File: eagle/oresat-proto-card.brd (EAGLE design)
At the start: 99.8 x 94.7 mm, 126 parts, among them J1 J-SAMTEC-TFM-110-X1-XXX-D-RA, J2 U.FL, J3 U.FL, J4 U.FL, J6 J-SAMTEC-TFM-120-X1-XXX-D-RA, J7 ORESAT-DEBUG-CONNECTOR-SOLAR, Q1 DMP2240UDM, Q3 MOSFET-PCH-SOT23-6, Q4 MOSFET-PCH-SOT23-6, Q5 PMV45EN, Q6 PMV45EN, U1 TCAN330, U3 MAX7310ATE, U4 MAX4211FETE, U5 TPS62111RSA, U7 STM32F091C, U8 MIC842LYC5, U9 MIC842LYC5, X2 16MHZ-2.5x2mm

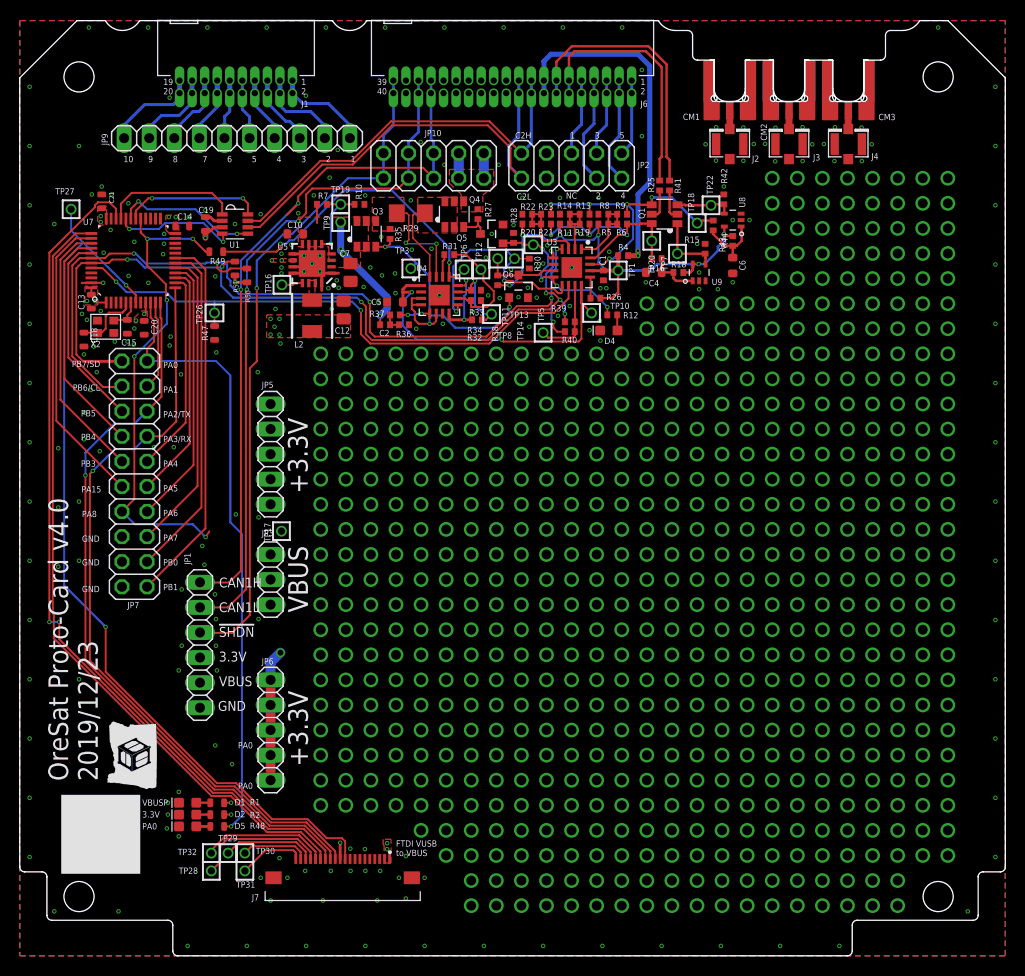
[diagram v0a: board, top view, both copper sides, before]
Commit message: swapped 0402 to 0603 where necessary, fixed labels on tnames layer
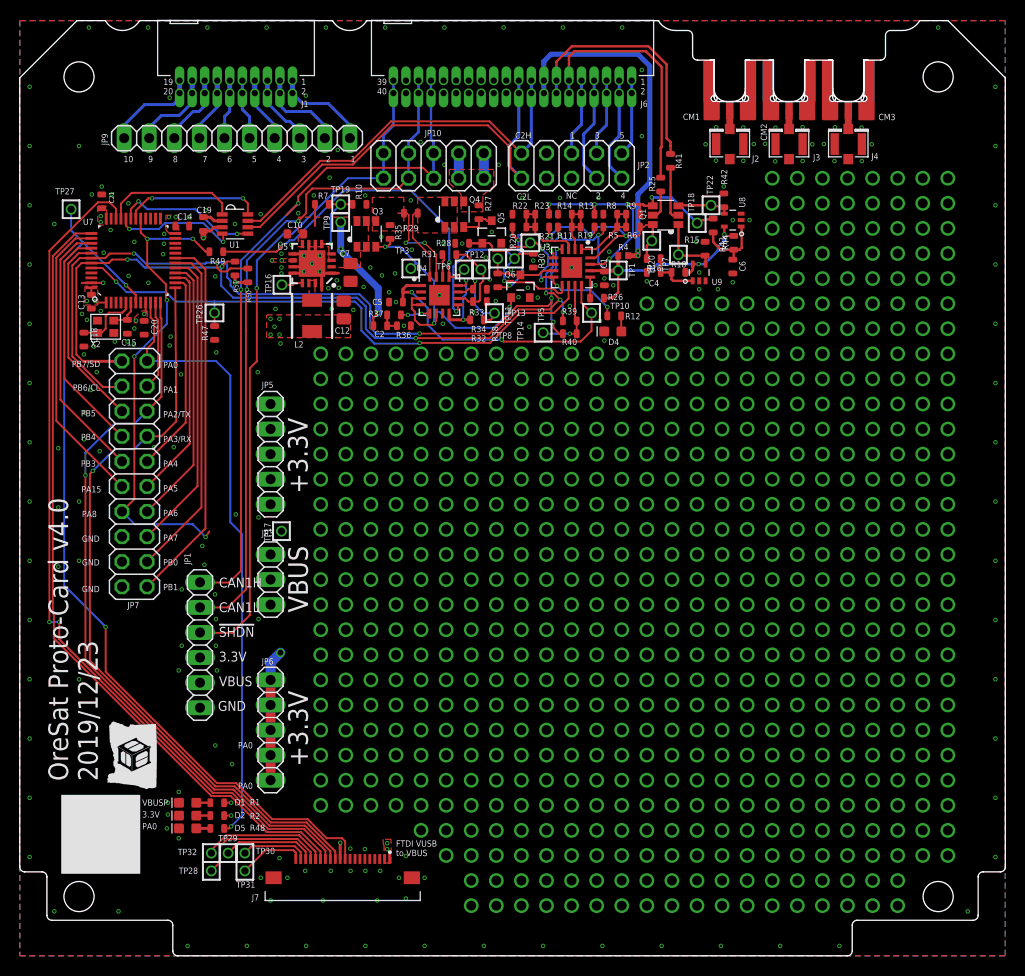
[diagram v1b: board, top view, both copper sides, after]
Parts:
- C1, C2, R10, R11, R12, R13, R14, R15, R16, R18, R19, R20, R21, R22, R23, R25, R26, R27, R28, R30, R31, R32, R33, R34, R35, R36, R37, R38, R39, R40, R41, R42, R43, R44, R5, R6, R7, R8, R9: device rcl_custom:.0402-B-NOSILK -> oresat-rcl:.0603-C-NOSILK
- C4, C5, C6: device oresat-rcl:.0603-B-NOSILK -> oresat-rcl:.0603-C-NOSILK
- R29: device rcl:R1206 -> oresat-rcl:.0603-C-NOSILK
- moved R28 5.23 mm to (44.8, 72.2), turned to 0 degrees
- moved R41 2.50 mm to (65.9, 80.5)
- moved R9 1.14 mm to (62.1, 73.8)
- moved R6 1.10 mm to (62.1, 75.1)
- moved R20 0.85 mm to (50.6, 73.8)
- moved R22 0.80 mm to (50.6, 75.1)
- moved R5 0.76 mm to (59.8, 73.8)
- moved R8 0.70 mm to (59.8, 75.1)
- moved C2 0.51 mm to (36.5, 63.8)
- moved R30 0.50 mm to (52.0, 70.4)
- moved R23 0.50 mm to (52.9, 73.8)
- moved R19 0.42 mm to (57.5, 73.8)
- moved D4 0.41 mm to (60.0, 63.2)
- moved R32 0.41 mm to (46.6, 66.2)
- moved R34 0.41 mm to (46.6, 67.5)
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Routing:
- net MAX4211-3V3: track 35.4 -> 30.9 mm
- net ON/!OFF: track 17.2 -> 21.6 mm
- net N$596: track 11.7 -> 8.90 mm
- net OPD_SCL: track 27.6 -> 25.0 mm
- net N$479: track 3.08 -> 5.48 mm
- net POUT: track 32.9 -> 34.0 mm
- net N$400: track 6.62 -> 7.47 mm
- net VBUSP: track 110.3 -> 109.4 mm
- net N$398: track 10.7 -> 9.93 mm
- net N$593: track 8.26 -> 7.54 mm
- net PB6/SCL: track 86.8 -> 86.2 mm
- net VPD: track 49.7 -> 50.4 mm
- net AD0: track 8.34 -> 9.01 mm
- net PB7/SDA: track 82.1 -> 81.4 mm
- net PEN-SDA-FILT: track 23.1 -> 23.7 mm
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
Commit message: updated design blocks, got rid of unneeded breakouts
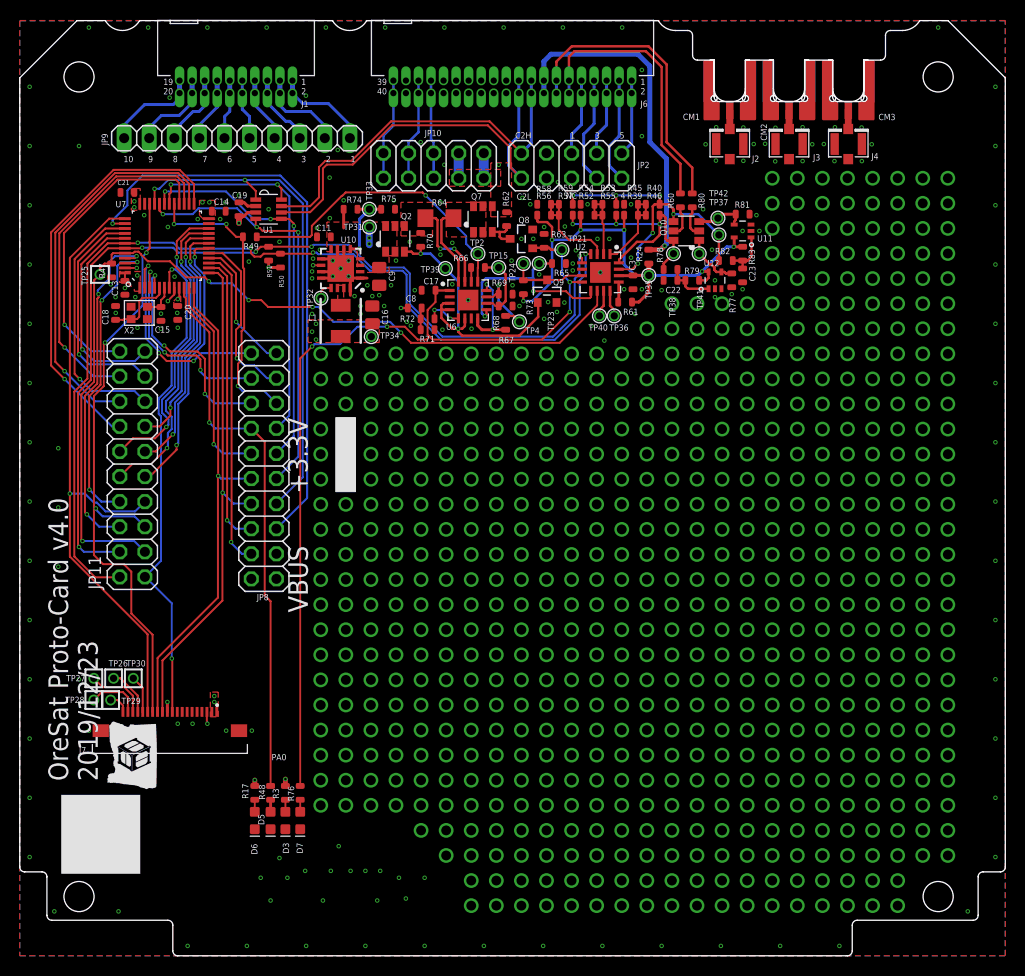
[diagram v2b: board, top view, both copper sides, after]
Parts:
- removed C1: 100n, oresat-rcl:.0603-C-NOSILK
- removed C10: 1u, oresat-rcl:.0603-B-NOSILK
- removed C12: 22u, oresat-rcl:.0805-B-NOSILK
- removed C2, R10, R11, R13, R14, R19, R20, R21, R22, R23, R32, R34, R36, R37, R5, R6, R8, R9: NP, oresat-rcl:.0603-C-NOSILK
- removed C4, C5, C6: 1u, oresat-rcl:.0603-C-NOSILK
- removed C7: 10u, oresat-rcl:.0805-B-NOSILK
- removed D1, D2: GREEN, SparkFun-LED:LED-0603
- removed D4: AMBER, SparkFun-LED:LED-0603
- removed JP1: (no value), pinhead:1X06
- removed JP3: (no value), pinhead:1X03
- removed JP5, JP6: (no value), pinhead:1X05
- removed JP7: (no value), pinhead:2X10
- removed L2: 6.8u, L-ECS-MPI4040:ECS-MPI4040
- removed Q1: DMP2240UDM, Q-MOSFET-PCH-dual-SOT23-6:SOT23-6
- removed Q3, Q4: MOSFET-PCH-SOT23-6, Q-MOSFET-PCH-SOT23-6:SOT23-6
- removed Q5, Q6: PMV45EN, Tova:SOT23
- removed R1, R12, R2: 2.7k, oresat-rcl:.0603-C-NOSILK
- removed R15, R26, R27, R28, R30, R35, R38, R42, R7: 10k, oresat-rcl:.0603-C-NOSILK
- removed R16, R43: 330k, oresat-rcl:.0603-C-NOSILK
- removed R18, R44: 1M, oresat-rcl:.0603-C-NOSILK
- removed R25, R41: 100, oresat-rcl:.0603-C-NOSILK
- removed R29: 100m, oresat-rcl:.0603-C-NOSILK
- removed R31, R33: 0, oresat-rcl:.0603-C-NOSILK
- removed R4: 100, rcl_custom:.0402-B-NOSILK
- removed TP1, TP10, TP11, TP12, TP13, TP14, TP16, TP17, TP18, TP19, TP20, TP22, TP3, TP5, TP6, TP7, TP8, TP9: TEST-POINT, Tova:2MM-TEST-POINT
- removed U3: MAX7310ATE, U-Maxim-MAX7310-I2C-GPIO-expander:QFN65P400X400X80-17T210
- removed U4: MAX4211FETE, U-Maxim-MAX4211-power-monitor:QFN65P400X400X80-17T210
- removed U5: TPS62111RSA, U-TI-TPS6211x-SPS-buck:S-PVQFN-16
- removed U8, U9: MIC842LYC5, U-Microchip-MIC842-Comparator:SC70-5
- added C11, C17, C22, C23: 1u, oresat-rcl:.0603-C-NOSILK
- added C16: 22u, oresat-rcl:.0805-B-NOSILK
- added C3: 100n, oresat-rcl:.0603-C-NOSILK
- added C8, R45, R46, R52, R53, R54, R55, R56, R57, R58, R59, R67, R69, R71, R72, R75: NP, oresat-rcl:.0603-C-NOSILK
- added C9: 10u, oresat-rcl:.0805-B-NOSILK
- added D3, D6: GREEN, SparkFun-LED:LED-0603
- added D7: AMBER, SparkFun-LED:LED-0603
- added JP11, JP8: (no value), pinhead:2X10
- added L1: 6.8u, L-ECS-MPI4040:ECS-MPI4040
- added Q10: DMP2240UDM, Q-MOSFET-PCH-dual-SOT23-6:SOT23-6
- added Q2, Q7: MOSFET-PCH-SOT23-6, Q-MOSFET-PCH-SOT23-6:SOT23-6
- added Q8, Q9: PMV45EN, Tova:SOT23
- added R17, R3, R76: 2.7k, oresat-rcl:.0603-C-NOSILK
- added R24: 10, oresat-rcl:.0603-C-NOSILK
- added R60, R80: 100, oresat-rcl:.0603-C-NOSILK
- added R61, R62, R63, R65, R70, R73, R74, R77, R81: 10k, oresat-rcl:.0603-C-NOSILK
- added R64: 100m, rcl:R1206
- added R66, R68: 0, oresat-rcl:.0603-C-NOSILK
- added R78, R82: 330k, oresat-rcl:.0603-C-NOSILK
- added R79, R83: 1M, oresat-rcl:.0603-C-NOSILK
- added TP15, TP2, TP21, TP23, TP24, TP33, TP34, TP35, TP36, TP37, TP38, TP39, TP4, TP40, TP41, TP42: TEST-POINT-LARGE-SQUARE, oresat-misc:1X01
- added TP25: TEST-POINT, Tova:2MM-TEST-POINT
- added U10: TPS62111RSA, U-TI-TPS6211x-SPS-buck:S-PVQFN-16
- added U11, U12: MIC842LYC5, U-Microchip-MIC842-Comparator:SC70-5
- added U2: MAX7310ATE, U-Maxim-MAX7310-I2C-GPIO-expander:QFN65P400X400X80-17T210
- added U6: MAX4211FETE, U-Maxim-MAX4211-power-monitor:QFN65P400X400X80-17T210
- R39, R40: value 47k -> NP
- TP31, TP32: value TEST-POINT -> TEST-POINT-LARGE-SQUARE; device Tova:2MM-TEST-POINT -> oresat-misc:1X01
- moved TP31 66.4 mm to (35.4, 73.8)
- moved TP32 57.3 mm to (30.5, 66.6), turned to 180 degrees
- moved TP27 47.6 mm to (7.50, 28.1)
- moved TP26 38.4 mm to (9.50, 28.1), turned to 0 degrees
- moved J7 23.0 mm to (15.2, 22.8)
- moved TP30 21.0 mm to (11.5, 28.1)
- moved TP28 21.0 mm to (7.50, 25.9)
- moved TP29 19.5 mm to (9.20, 25.9)
- moved R40 15.6 mm to (64.1, 76.1)
- moved R39 12.4 mm to (61.9, 75.0)
- moved R47 12.2 mm to (9.30, 69.4)
- moved D5 8.44 mm to (25.4, 13.7), turned to 270 degrees
- moved R48 6.49 mm to (25.4, 16.5), turned to 90 degrees
- moved C18 4.19 mm to (9.70, 65.1), turned to 90 degrees
- moved C14 3.99 mm to (20.1, 75.4)
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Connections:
- removed net CAN_SILENT: U1.8, U7.30
- removed net IOUT: R31.2, U4.14
- removed net MAX4211-3V3: C5.1, TP10.1, U3.12, U4.1
- removed net N$270: D1.A, R1.1
- removed net N$271: D2.A, R2.1
- removed net N$385: R39.1, R40.1, TP5.1, U3.11
- removed net N$398: Q3.4, R29.2, R35.2, U4.15
- removed net N$400: C6.1, R43.1, R44.1, U8.1
- removed net N$401: C4.1, R16.1, R18.1, U9.1
- removed net N$479: Q1.2, R41.2
- removed net N$480: Q1.3, R42.2, TP22.1, U8.4
- removed net N$527: J7.16, TP32.1
- removed net N$575: D4.A, R12.1
- removed net N$579: Q1.5, R25.2
- removed net N$580: Q1.1, R15.2, TP7.1, U9.4
- removed net N$589: R26.1, U3.13
- removed net N$590: Q4.3, Q5.3, R27.1
- removed net N$593: Q4.1, Q4.2, Q4.5, Q4.6, R29.1, U4.16
- removed net N$596: R31.1, R32.2, TP12.1, U4.10
- removed net N$597: R33.1, R34.2, TP11.1, U4.11
- removed net N$599: R33.2, U4.12, U4.8
- removed net N$603: C2.1, R36.2, R37.2
- removed net N$604: R37.1, U4.5
- removed net POUTPROT: JP7.13, R49.2, U7.29
- removed net TPS62111-PG: TP16.1, U5.13
- removed net TPS62111-SYNC: R10.2, R7.1, TP19.1, U5.5
- removed net TPS62111_SW: L2.1, U5.14, U5.15
- new net IOUT1: R66.2, U6.14
- new net N$518: D3.A, R3.1
- new net N$519: D6.A, R17.1
- new net N$520: R61.1, U2.13
- new net N$522: J7.20, TP29.1
- new net N$529: Q7.3, Q8.3, R62.1
- new net N$530: Q7.1, Q7.2, Q7.5, Q7.6, R64.1, U6.16
- new net N$531: R66.1, R67.2, TP15.1, U6.10
- new net N$532: R68.1, R69.2, TP4.1, U6.11
- new net N$533: R68.2, U6.12, U6.8
- new net N$534: R72.1, U6.5
- new net N$535: C8.1, R71.2, R72.2
- new net N$536: Q2.4, R64.2, R70.2, U6.15
- new net N$537: D7.A, R76.1
- new net N$538: Q10.5, R60.2
- new net N$539: Q10.1, R77.2, TP41.1, U12.4
- new net N$540: TP40.1, U2.11
- new net N$541: Q10.2, R80.2
- new net N$573: Q10.3, R81.2, TP42.1, U11.4
- new net N$574: C23.1, R82.1, R83.1, U11.1
- new net N$578: C22.1, R78.1, R79.1, U12.1
- new net N$581: TP36.1, U2.12
- new net PA8/POUTPROT: JP8.6, R49.2, U7.29
- new net PA9/CAN_SILENT: JP8.8, U1.8, U7.30
- new net PB10: JP11.10, U7.21
- new net PB11: JP11.12, U7.22
- new net PB12: JP11.14, U7.25
- new net PB13: JP11.16, U7.26
- new net PB14: JP11.18, U7.27
- new net PB15: JP11.20, U7.28
- new net PB2: JP11.13, U7.20
- new net PB8: JP11.6, U7.45
- new net PB9: JP11.8, U7.46
- new net PC13: JP8.1, U7.2
- new net PC14: JP8.3, U7.3
- new net PC15: JP8.5, U7.4
- new net TPS62111-PG1: TP32.1, U10.13
- new net TPS62111-SYNC1: R74.1, R75.2, TP33.1, U10.5
- new net TPS62111_SW3: L1.1, U10.14, U10.15
- net !FAULT: now also Q9.3, R73.1, TP24.1, U2.7; no longer Q6.3, R38.1, TP8.1, U3.7
- net !SD: no longer JP1.3
- net 3.3V: now also C16.1, L1.2, R17.2, TP34.1, U10.10; no longer C12.1, JP1.4, JP5.1, JP5.2, JP5.3, JP5.4, JP5.5, JP6.1, JP6.2, JP6.3, JP6.4, JP6.5, L2.2, R2.2, TP17.1, U5.10
- net AD0: now also R39.1, R40.2, R45.2, R46.1, U2.1; no longer R5.1, R6.2, R8.2, R9.1, U3.1
- net AD1: now also R52.1, R53.2, R54.2, R55.1, U2.2; no longer R11.1, R13.2, R14.2, R19.1, U3.2
- net AD2: now also R56.1, R57.2, R58.2, R59.1, U2.3; no longer R20.1, R21.2, R22.2, R23.1, U3.3
- net BOOT0: now also JP11.3, TP25.1, U2.10; no longer TP26.1, U3.10
- net CAN1_H: no longer JP1.1
- net CAN1_L: no longer JP1.2
- net CAN_RX: now also JP8.12
- net CAN_SHDN: now also JP8.10
- net CAN_TX: now also JP8.14
- net CB-RESET: now also R65.2, TP23.1, U2.9, U6.9; no longer R30.2, TP14.1, U3.9, U4.9
- net CB_CTRL: now also Q2.3, Q9.1, R70.1, TP39.1, U6.3, U6.4, U6.6; no longer Q3.3, Q6.1, R35.1, TP3.1, U4.3, U4.4, U4.6
- net GND: now also C11.2, C16.2, C17.2, C22.2, C23.2, C3.1, C9.2, D3.C, D6.C, D7.C, JP8.19, Q8.2, Q9.2, R45.1, R54.1, R58.1, R63.1, R65.1, R67.1, R69.1, R71.1, R75.1, R77.1, R81.1, U10.1, U10.11, U10.12, U10.16, U10.6, U10.7, U10.9, U10.PAD, U11.2, U12.2, U2.6, U2.EPAD, U6.7, U6.EPAD; no longer C1.1, C10.2, C12.2, C4.2, C5.2, C6.2, C7.2, D1.C, D2.C, D4.C, JP1.6, JP7.15, JP7.17, JP7.19, Q5.2, Q6.2, R10.1, R14.1, R15.1, R22.1, R28.1, R30.1, R32.1, R34.1, R36.1, R42.1, R8.1, U3.6, U3.EPAD, U4.7, U4.EPAD, U5.1, U5.11, U5.12, U5.16, U5.6, U5.7, U5.9, U5.PAD, U8.2, U9.2
- net N$523: now also J7.19, TP28.1; no longer J7.20, TP31.1
- net N$524: now also J7.18, TP27.1; no longer J7.19, TP30.1
- net N$525: now also J7.17, TP26.1; no longer J7.18, TP29.1
- net N$526: now also J7.16, TP30.1; no longer J7.17, TP28.1
- net NRESET: now also JP11.1; no longer TP27.1
- net ON/!OFF: now also C17.1, Q8.1, R63.2, R76.2, TP21.1, U2.8, U6.1; no longer Q5.1, R12.2, R28.2, TP13.1, U3.8
- net OPD_PWR: now also R24.1; no longer R4.1
- net OPD_SCL: now also R80.1; no longer R41.1
- net OPD_SDA: now also R60.1; no longer R25.1
- net PA0: now also JP8.7; no longer JP7.2
- net PA1: now also JP8.9; no longer JP7.4
- net PA15: now also JP8.16; no longer JP7.11
- net PA2/USART2_TX: now also JP8.11; no longer JP7.6
- net PA3/USART2_RX: now also JP8.13; no longer JP7.8
- net PA4: now also JP8.15; no longer JP7.10
- net PA5/SPI1_SCK: now also JP8.17; no longer JP7.12
- net PA6/SPI1_MISO: now also JP8.2; no longer JP7.14
- net PA7/SPI1_MOSI: now also JP8.4; no longer JP7.16
- net PB0: now also JP11.9; no longer JP7.18
- net PB1: now also JP11.11; no longer JP7.20
- net PB3: now also JP11.15; no longer JP7.9
- net PB4: now also JP11.17; no longer JP7.7
- net PB5: now also JP11.19; no longer JP7.5
- net PB6/SCL: now also JP11.2, U2.4; no longer JP7.3, R40.2, U3.4
- net PB7/SDA: now also JP11.4, U2.5; no longer JP7.1, R39.2, U3.5
- net PEN-SCL-FILT: now also Q10.4, R40.1, R53.1, R57.1, R82.2, TP37.1, U2.15; no longer Q1.4, R13.1, R21.1, R43.2, R6.1, TP18.1, U3.15
- net PEN-SDA-FILT: now also Q10.6, R46.2, R55.2, R59.2, R78.2, TP38.1, U2.16; no longer Q1.6, R16.2, R19.2, R23.2, R9.2, TP20.1, U3.16
- net POUT: now also TP2.1, U6.13; no longer TP6.1, U4.13
- net SWCLK: now also JP11.7
- net SWDIO: now also JP11.5
- net VBUS: now also Q7.4, R62.2; no longer Q4.4, R27.2
- net VBUSP: now also C11.1, C8.2, C9.1, Q2.1, Q2.2, Q2.5, Q2.6, R3.2, R74.2, TP31.1, U10.2, U10.3, U10.4, U10.8; no longer C10.1, C2.2, C7.1, JP1.5, JP3.1, JP3.2, JP3.3, Q3.1, Q3.2, Q3.5, Q3.6, R1.2, R7.2, TP9.1, U5.2, U5.3, U5.4, U5.8
- net VPD: now also C3.2, R24.2, R39.2, R52.2, R56.2, R61.2, R73.2, R79.2, R83.2, TP35.1, U11.5, U12.5, U2.14; no longer C1.2, R11.2, R18.2, R20.2, R26.2, R38.2, R4.2, R44.2, R5.2, TP1.1, U3.14, U8.5, U9.5
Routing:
- net ON/!OFF: track 21.6 -> 91.4 mm
- net CAN1_H: track 72.0 -> 10.00 mm, vias 2 -> 0
- net CAN1_L: track 70.0 -> 10.3 mm, vias 2 -> 0
- net !SD: track 68.6 -> 10.3 mm, vias 1 -> 0
- net POUTPROT: track 49.7 -> 0.00 mm, vias 5 -> 0
- net PB12: track 0.00 -> 42.7 mm, vias 0 -> 1
- net NRESET: track 91.8 -> 50.7 mm
- net PA9/CAN_SILENT: track 0.00 -> 40.2 mm, vias 0 -> 2
- net PB13: track 0.00 -> 39.8 mm, vias 0 -> 1
- net CAN_TX: track 13.8 -> 51.8 mm, vias 0 -> 2
- net PB14: track 0.00 -> 36.0 mm, vias 0 -> 1
- net BOOT0: track 58.5 -> 93.7 mm, vias 2 -> 5
- net PB8: track 0.00 -> 34.8 mm, vias 0 -> 3
- net PB10: track 0.00 -> 32.2 mm, vias 0 -> 2
- net PB15: track 0.00 -> 32.2 mm, vias 0 -> 1
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- added copper zone on layer 1, net N$530
- added copper zone on layer 1, net N$536
- added copper zone on layer 1, net TPS62111_SW3
- removed copper zone on layer 1, net N$398
- removed copper zone on layer 1, net N$593
- removed copper zone on layer 1, net TPS62111_SW
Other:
- board text removed: "!SHDN"
- board text removed: "3.3V"
- board text removed: "CAN1H"
- board text removed: "CAN1L"
- board text removed: "FTDI VUSB to VBUS"
- board text removed: "GND"
- board text removed: "PA1"
- board text removed: "PA15"
- board text removed: "PA2/TX"
- board text removed: "PA3/RX"
- board text removed: "PA4"
- board text removed: "PA5"
- board text removed: "PA6"
- board text removed: "PA7"
- board text removed: "PA8"
- board text removed: "PB0"
- board text removed: "PB1"
- board text removed: "PB3"
- board text removed: "PB4"
- board text removed: "PB5"
- board text removed: "PB6/CL"
- board text removed: "PB7/SD"
- board text removed: "VBUSP"

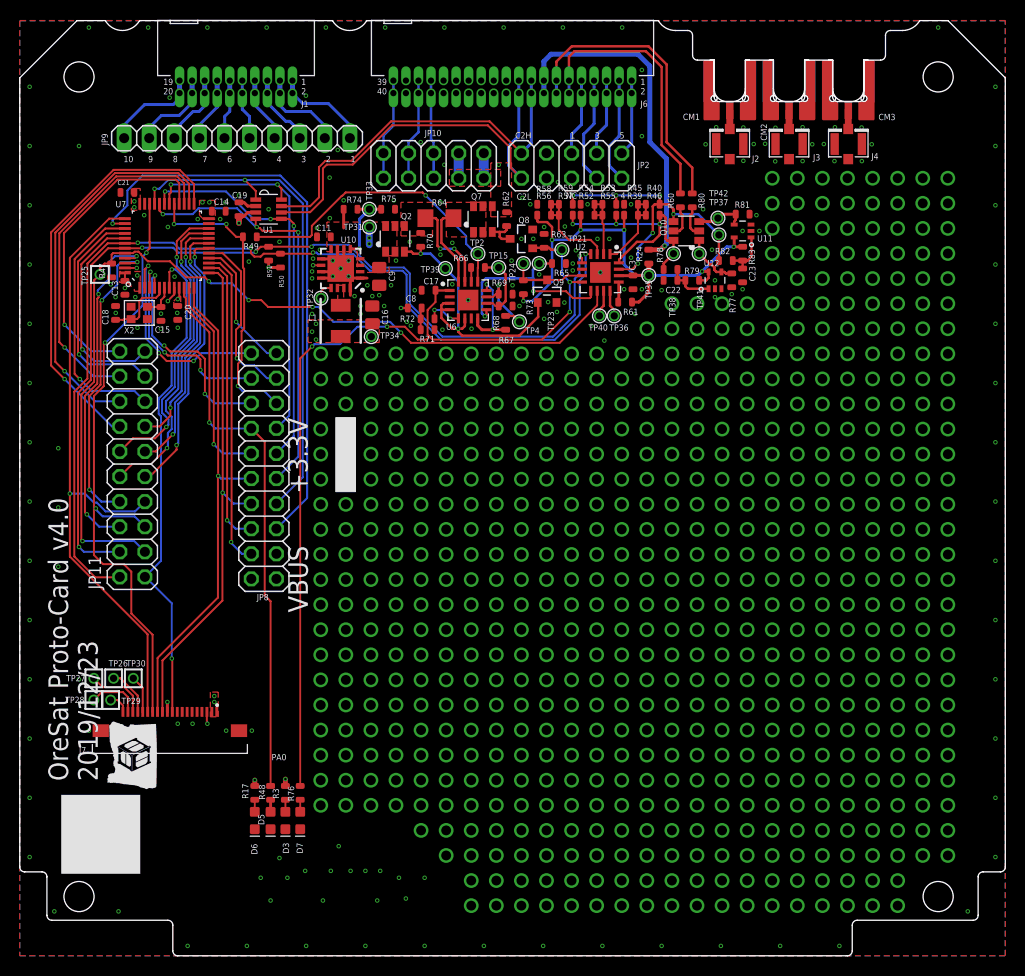
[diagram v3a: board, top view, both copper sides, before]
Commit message: moved ffc to bottom of card, fixed silkscreen, moved and expanded Vbus and 3.3V breakouts
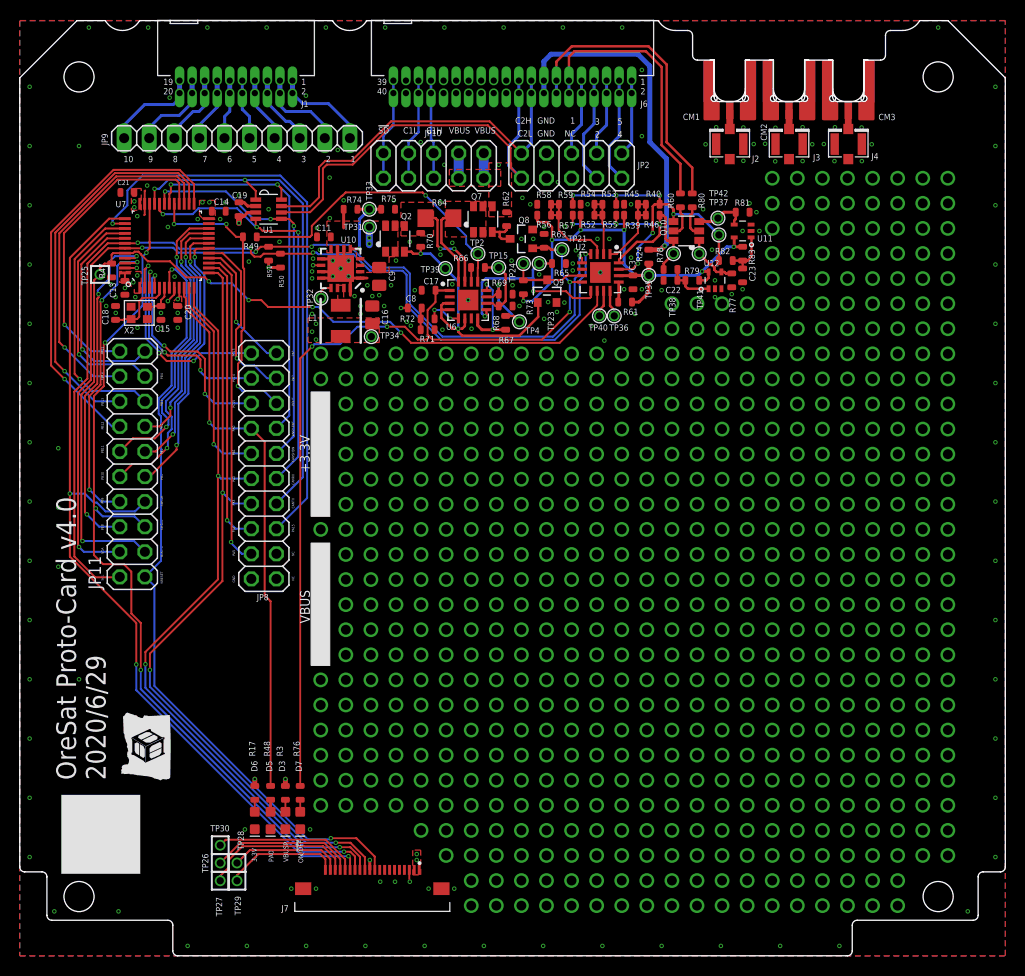
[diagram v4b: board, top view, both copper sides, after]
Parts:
- moved J7 26.0 mm to (35.7, 6.80)
- moved TP27 24.2 mm to (20.3, 7.60)
- moved TP29 22.3 mm to (22.0, 7.60)
- moved TP28 22.0 mm to (22.0, 9.40)
- moved TP26 21.6 mm to (20.3, 9.40)
- moved TP30 19.1 mm to (20.3, 11.2)
- moved R81 0.20 mm to (73.2, 75.3)
- moved C15 0.10 mm to (14.3, 65.1)
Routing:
- net PA2/USART2_TX: track 50.0 -> 78.2 mm, vias 1 -> 3
- net PA3/USART2_RX: track 51.5 -> 79.6 mm, vias 1 -> 3
- net NRESET: track 50.7 -> 78.3 mm
- net SWDIO: track 63.6 -> 90.9 mm, vias 3 -> 5
- net SWCLK: track 65.2 -> 92.4 mm, vias 1 -> 3
- net N$526: track 3.79 -> 14.8 mm
- net N$525: track 4.82 -> 14.8 mm
- net N$522: track 2.13 -> 11.7 mm
- net N$524: track 6.32 -> 15.5 mm
- net VBUSP: track 101.5 -> 108.7 mm, vias 9 -> 11
- net N$523: track 5.49 -> 11.5 mm
- net GND: track 21.5 -> 24.1 mm, vias 305 -> 285
- net 3.3V: track 9.41 -> 9.51 mm, vias 18 -> 22
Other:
- board text added: "!SD"
- board text added: "2020/6/29"
- board text added: "3.3V"
- board text added: "BOOT0"
- board text added: "C1H"
- board text added: "C1L"
- board text added: "CANRX"
- board text added: "CANSHDN"
- board text added: "CANSILENT"
- board text added: "CANTX"
- board text added: "GND"
- board text added: "NRESET"
- board text added: "ON/!OFF"
- board text added: "PA1"
- board text added: "PA15"
- board text added: "PA2"
- board text added: "PA3"
- board text added: "PA4"
- board text added: "PA5"
- board text added: "PA6"
- board text added: "PA7"
- board text added: "PB0"
- board text added: "PB1"
- board text added: "PB10"
- board text added: "PB11"
- board text added: "PB12"
- board text added: "PB13"
- board text added: "PB14"
- board text added: "PB15"
- board text added: "PB2"
- board text added: "PB3"
- board text added: "PB4"
- board text added: "PB6"
- board text added: "PB8"
- board text added: "PB9"
- board text added: "PC13"
- board text added: "PC14"
- board text added: "PC15"
- board text added: "POUT"
- board text added: "SCL"
- board text added: "SDA"
- board text added: "SWCLK"
- board text added: "SWDIO"
- board text added: "VBUSP"
- board text removed: "2019/12/23"
